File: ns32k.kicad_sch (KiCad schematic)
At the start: 52 parts, among them SW2 SW_DIP_x04, U1 NS32201, U10 74AHC373, U11 74AHC373, U12 74AHC138, U13 AS6C6416-55, U15 MX29LV040C, U16 MX29LV040C, U19 74AHC138, U20 74AHC1G08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

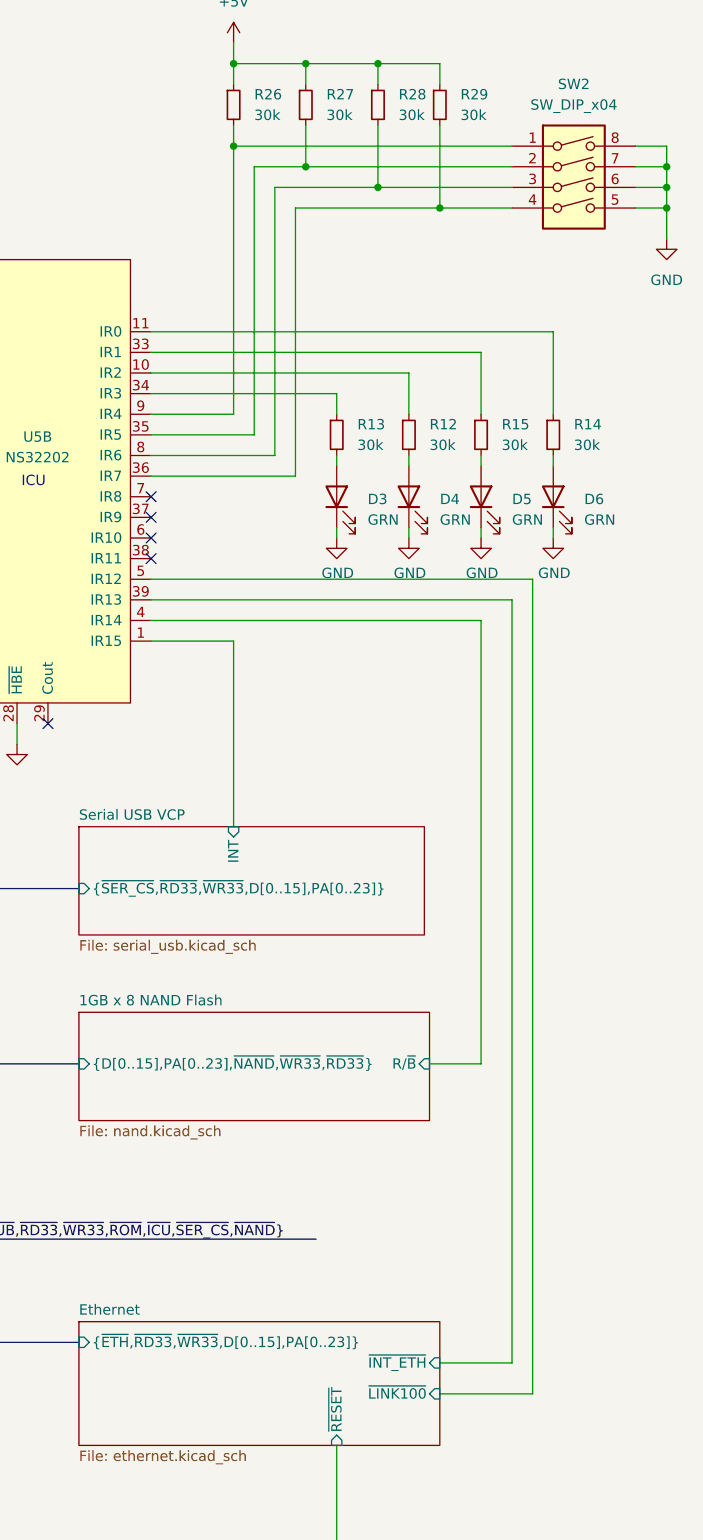
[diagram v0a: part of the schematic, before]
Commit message: use ICU even pins for GPIO
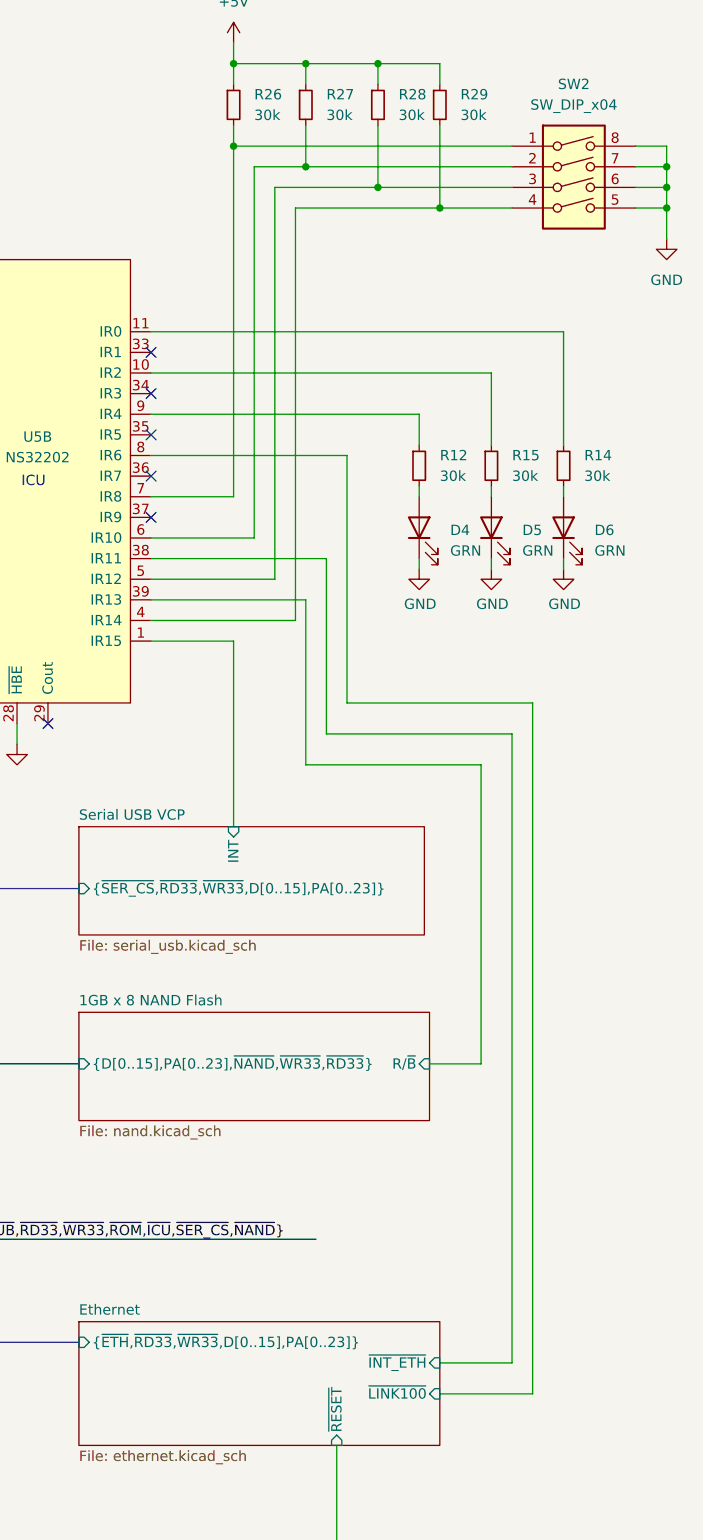
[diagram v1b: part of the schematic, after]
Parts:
- removed D3: GRN, Diode_SMD:D_0603_1608Metric, symbol Device:LED
- removed R13: 30k, Resistor_SMD:R_0402_1005Metric, symbol Device:R_Small
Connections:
- net 1GB x 8 NAND Flash/R/~{B}: now also U5.39 (IR13); no longer U5.4 (IR14)
- net Ethernet/~{INT_ETH}: now also U5.38 (IR11); no longer U5.39 (IR13)
- net Ethernet/~{LINK100}: now also U5.8 (IR6); no longer U5.5 (IR12)
- net at R26.2, SW2.1: now also U5.7 (IR8); no longer U5.9 (IR4)
- net at R27.2, SW2.2: now also U5.6 (IR10); no longer U5.35 (IR5)
- net at R28.2, SW2.3: now also U5.5 (IR12); no longer U5.8 (IR6)
- net at R29.2, SW2.4: now also U5.4 (IR14); no longer U5.36 (IR7)
- net at R15.1: now also U5.10 (IR2); no longer U5.33 (IR1)
- net at R12.1: now also U5.9 (IR4); no longer U5.10 (IR2)
- no-connect marks 18 -> 19
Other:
- moved on the sheet: D4, D5, D6, R12, R14, R15

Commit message: add jumpers, much cleanup
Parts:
- added R13, R41: 0R, Resistor_SMD:R_0402_1005Metric, symbol Device:R_Small
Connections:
- net PA5: now also R41.1
- net ST1: now also R13.1; no longer U5.3 (ST1)
- new net: R13.2, R41.2, U5.3 (ST1)
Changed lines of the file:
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@@
 	)
 	(junction
+		(at 290.83 52.07)
+		(diameter 0)
+		(color 0 0 0 0)
+	)
+	(junction
 		(at 219.71 151.13)
 		(diameter 0)
@@
 	)
 	(bus_entry
+		(at 293.37 73.66)
+		(size -2.54 -2.54)
+		(stroke
+			(width 0)
+			(type default)
+		)
+	)
+	(bus_entry
 		(at 205.74 114.3)
 		(size 2.54 2.54)
@@
 	)
 	(bus_entry
-		(at 270.51 76.2)
+		(at 245.11 76.2)
 		(size 2.54 -2.54)
 		(stroke
@@
 	(bus
 		(pts
-			(xy 262.89 76.2) (xy 265.43 76.2)
-		)
-		(stroke
-			(width 0)
-			(type default)
-		)
-	)
-	(bus
-		(pts
 			(xy 293.37 125.73) (xy 293.37 114.3)
 		)
@@
 	(bus
 		(pts
+			(xy 267.97 76.2) (xy 271.78 76.2)
+		)
+		(stroke
+			(width 0)
+			(type default)
+		)
+	)
+	(bus
+		(pts
 			(xy 106.68 76.2) (xy 109.22 76.2)
 		)
@@
 		)
 	)
+	(bus
+		(pts
+			(xy 266.7 76.2) (xy 267.97 76.2)
+		)
+		(stroke
+			(width 0)
+			(type default)
+		)
+	)
 	(wire
 		(pts
@@
 	(bus
 		(pts
-			(xy 293.37 72.39) (xy 293.37 74.93)
+			(xy 293.37 72.39) (xy 293.37 73.66)
 		)
 		(stroke
@@
 	(bus
 		(pts
-			(xy 220.98 76.2) (xy 250.19 76.2)
+			(xy 220.98 76.2) (xy 245.11 76.2)
 		)
 		(stroke
@@
 		)
 	)
+	(wire
+		(pts
+			(xy 290.83 52.07) (xy 303.53 52.07)
+		)
+		(stroke
+			(width 0)
+			(type default)
+		)
+	)
 	(bus
 		(pts
@@
 		)
 	)
+	(bus
+		(pts
+			(xy 250.19 76.2) (xy 245.11 76.2)
+		)
+		(stroke
+			(width 0)
+			(type default)
+		)
+	)
 	(wire
 		(pts
@@
 		)
 	)
-	(bus
-		(pts
-			(xy 266.7 76.2) (xy 267.97 76.2)
-		)
-		(stroke
-			(width 0)
-			(type default)
-		)
-	)
 	(wire
 		(pts
@@
 		)
 	)
-	(bus
-		(pts
-			(xy 250.19 76.2) (xy 252.73 76.2)
-		)
-		(stroke
-			(width 0)
-			(type default)
-		)
-	)
 	(wire
 		(pts
@@
 	(bus
 		(pts
+			(xy 252.73 76.2) (xy 250.19 76.2)
+		)
+		(stroke
+			(width 0)
+			(type default)
+		)
+	)
+	(bus
+		(pts
 			(xy 190.5 246.38) (xy 193.04 246.38)
 		)
@@
 		)
 	)
-	(bus
-		(pts
-			(xy 252.73 76.2) (xy 255.27 76.2)
-		)
-		(stroke
-			(width 0)
-			(type default)
-		)
-	)
 	(wire
 		(pts
@@
 	(bus
 		(pts
-			(xy 267.97 76.2) (xy 270.51 76.2)
-		)
-		(stroke
-			(width 0)
-			(type default)
-		)
-	)
-	(bus
-		(pts
 			(xy 139.7 114.3) (xy 142.24 114.3)
 		)
@@
 		)
 	)
+	(wire
+		(pts
+			(xy 290.83 52.07) (xy 290.83 58.42)
+		)
+		(stroke
+			(width 0)
+			(type default)
+		)
+	)
 	(bus
 		(pts
@@
 		)
 	)
+	(wire
+		(pts
+			(xy 255.27 52.07) (xy 290.83 52.07)
+		)
+		(stroke
+			(width 0)
+			(type default)
+		)
+	)
 	(bus
 		(pts
@@
 	(bus
 		(pts
-			(xy 270.51 76.2) (xy 271.78 76.2)
-		)
-		(stroke
-			(width 0)
-			(type default)
-		)
-	)
-	(bus
-		(pts
 			(xy 162.56 76.2) (xy 163.83 76.2)
 		)
@@
 		)
 	)
+	(bus
+		(pts
+			(xy 255.27 76.2) (xy 252.73 76.2)
+		)
+		(stroke
+			(width 0)
+			(type default)
+		)
+	)
 	(wire
 		(pts
@@
 	(bus
 		(pts
+			(xy 265.43 76.2) (xy 262.89 76.2)
+		)
+		(stroke
+			(width 0)
+			(type default)
+		)
+	)
+	(bus
+		(pts
 			(xy 157.48 76.2) (xy 158.75 76.2)
 		)
@@
 	(wire
 		(pts
-			(xy 273.05 52.07) (xy 303.53 52.07)
+			(xy 247.65 52.07) (xy 250.19 52.07)
 		)
 		(stroke
@@
 		)
 	)
+	(bus
+		(pts
+			(xy 257.81 76.2) (xy 255.27 76.2)
+		)
+		(stroke
+			(width 0)
+			(type default)
+		)
+	)
 	(wire
 		(pts
@@
 	(wire
 		(pts
+			(xy 290.83 63.5) (xy 290.83 71.12)
+		)
+		(stroke
+			(width 0)
+			(type default)
+		)
+	)
+	(bus
+		(pts
+			(xy 293.37 73.66) (xy 293.37 74.93)
+		)
+		(stroke
+			(width 0)
+			(type default)
+		)
+	)
+	(wire
+		(pts
 			(xy 355.6 24.13) (xy 355.6 26.67)
 		)
@@
 	(wire
 		(pts
-			(xy 273.05 73.66) (xy 273.05 52.07)
+			(xy 247.65 73.66) (xy 247.65 52.07)
 		)
 		(stroke
@@
 		)
 	)
-	(bus
-		(pts
-			(xy 255.27 76.2) (xy 257.81 76.2)
-		)
-		(stroke
-			(width 0)
-			(type default)
-		)
-	)
 	(wire
 		(pts
@@
 		)
 	)
+	(label "PA5"
+		(at 290.83 71.12 90)
+		(effects
+			(font
+				(size 1.27 1.27)
+			)
+			(justify left bottom)
+		)
+	)
 	(label "D6"
 		(at 118.11 123.19 0)
@@
 	)
 	(label "ST1"
-		(at 273.05 72.39 90)
+		(at 247.65 72.39 90)
 		(fields_autoplaced yes)
 		(effects
@@
 	)
 	(symbol
+		(lib_id "Device:R_Small")
+		(at 252.73 52.07 90)
+		(unit 1)
+		(exclude_from_sim no)
+		(in_bom yes)
+		(on_board yes)
+		(dnp no)
+		(fields_autoplaced yes)
+		(property "Reference" "R13"
+			(at 252.73 46.99 90)
+			(effects
+				(font
+					(size 1.27 1.27)
+				)
+			)
+		)
+		(property "Value" "0R"
+			(at 252.73 49.53 90)
+			(effects
+				(font
+					(size 1.27 1.27)
+				)
+			)
+		)
+		(property "Footprint" "Resistor_SMD:R_0402_1005Metric"
+			(at 252.73 52.07 0)
+			(effects
+				(font
+					(size 1.27 1.27)
+				)
+				(hide yes)
+			)
+		)
+		(property "Datasheet" "~"
+			(at 252.73 52.07 0)
+			(effects
+				(font
+					(size 1.27 1.27)
+				)
+				(hide yes)
+			)
+		)
+		(property "Description" "Resistor, small symbol"
+			(at 252.73 52.07 0)
+			(effects
+				(font
+					(size 1.27 1.27)
+				)
+				(hide yes)
+			)
+		)
+		(pin "1"
+		)
+		(pin "2"
+		)
+		(instances
+			(project "ns32k"
+				(path "/54787df0-1b8c-465f-acae-f55ec7f02da3"
+					(reference "R13")
+					(unit 1)
+				)
+			)
+		)
+	)
+	(symbol
 		(lib_id "NS32K_chipset:NS32202")
 		(at 322.58 67.31 0)
@@
 					(unit 1)
 				)
+			)
+		)
+	)
+	(symbol
+		(lib_id "Device:R_Small")
+		(at 290.83 60.96 0)
+		(mirror x)
+		(unit 1)
+		(exclude_from_sim no)
+		(in_bom yes)
+		(on_board yes)
+		(dnp yes)
+		(property "Reference" "R41"
+			(at 288.29 59.6899 0)
+			(effects
+				(font
+					(size 1.27 1.27)
+				)
+				(justify right)
+			)
+		)
+		(property "Value" "0R"
+			(at 288.29 62.2299 0)
+			(effects
+				(font
+					(size 1.27 1.27)
+				)
+				(justify right)
+			)
+		)
+		(property "Footprint" "Resistor_SMD:R_0402_1005Metric"
+			(at 290.83 60.96 0)
+			(effects
+				(font
+					(size 1.27 1.27)
+				)
+				(hide yes)
+			)
+		)
+		(property "Datasheet" "~"
+			(at 290.83 60.96 0)
+			(effects
+				(font
+					(size 1.27 1.27)
+				)
+				(hide yes)
+			)
+		)
+		(property "Description" "Resistor, small symbol"
+			(at 290.83 60.96 0)
+			(effects
+				(font
+					(size 1.27 1.27)
+				)
+				(hide yes)
+			)
+		)
+		(pin "1"
+		)
+		(pin "2"
+		)
+		(instances
+			(project "ns32k"
+				(path "/54787df0-1b8c-465f-acae-f55ec7f02da3"
+					(reference "R41")
+					(unit 1)
+				)

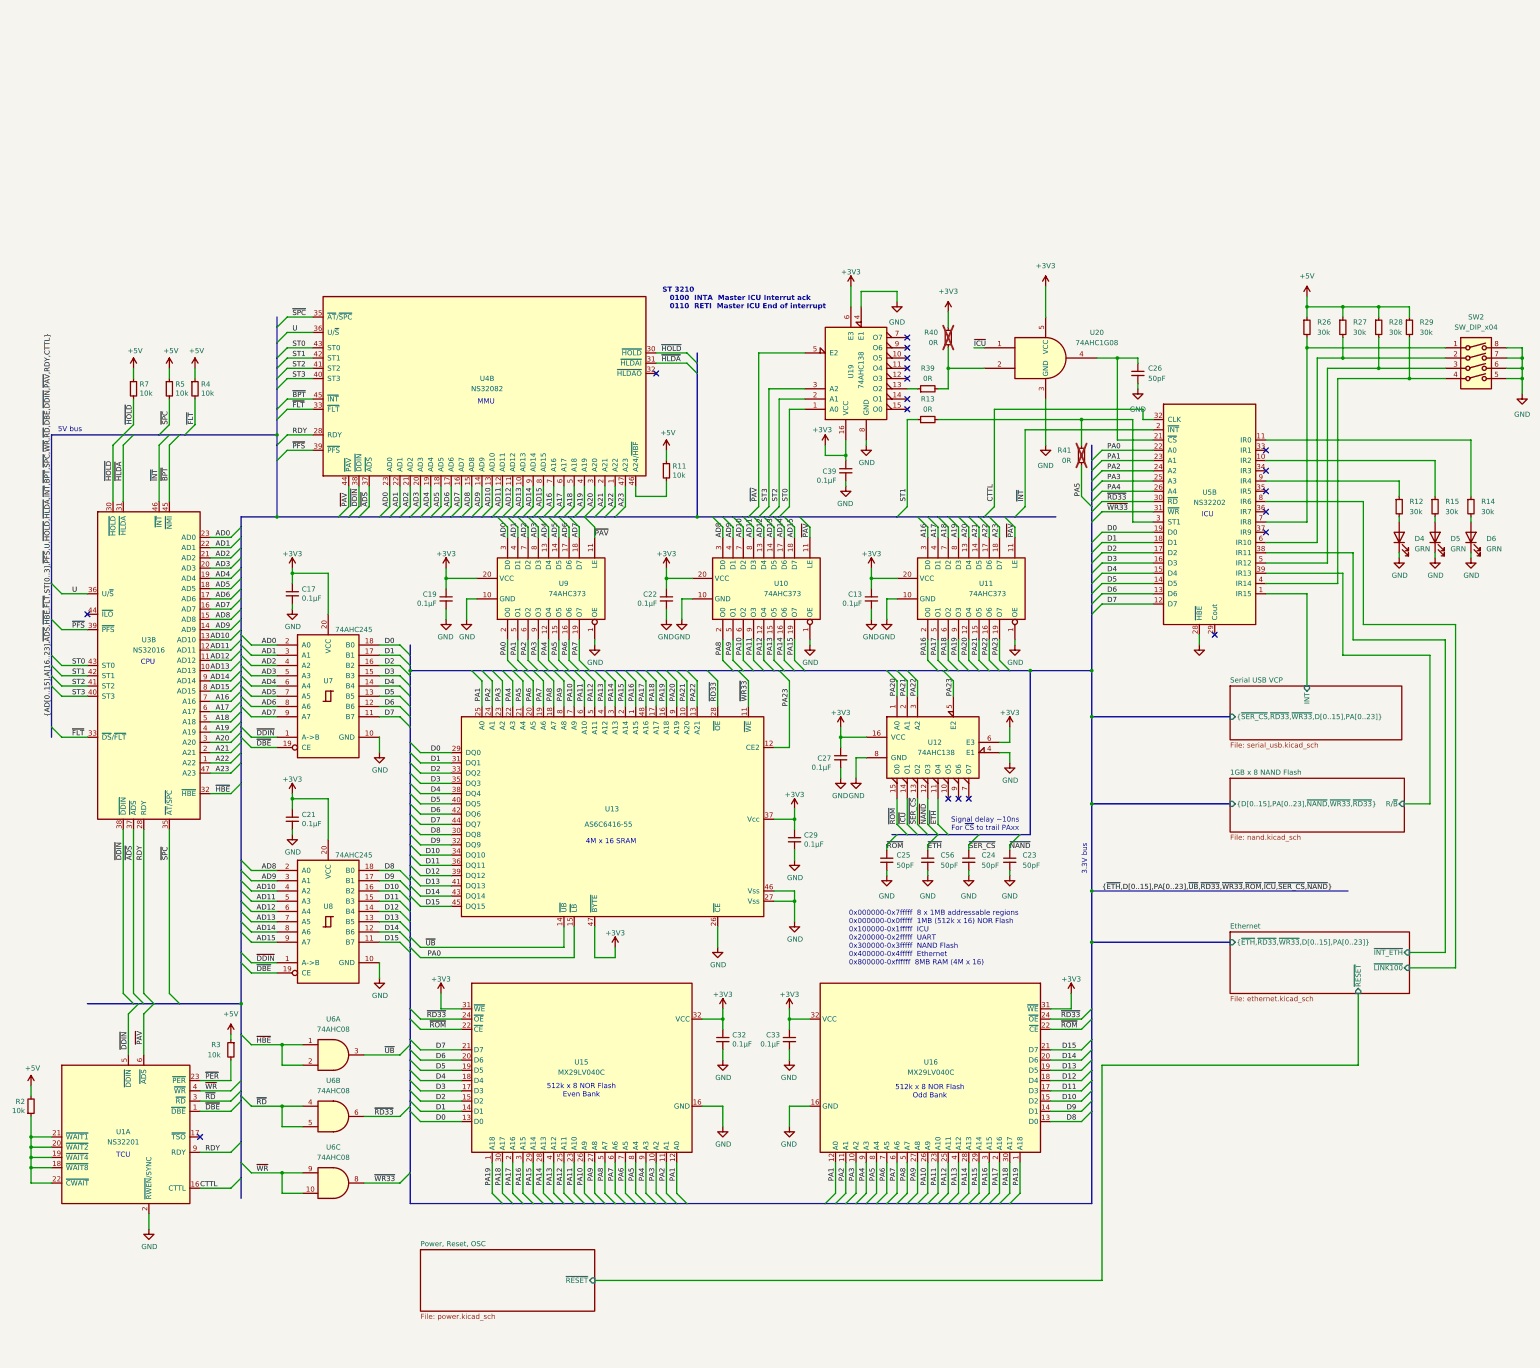
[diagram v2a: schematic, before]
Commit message: add buffer to ICU
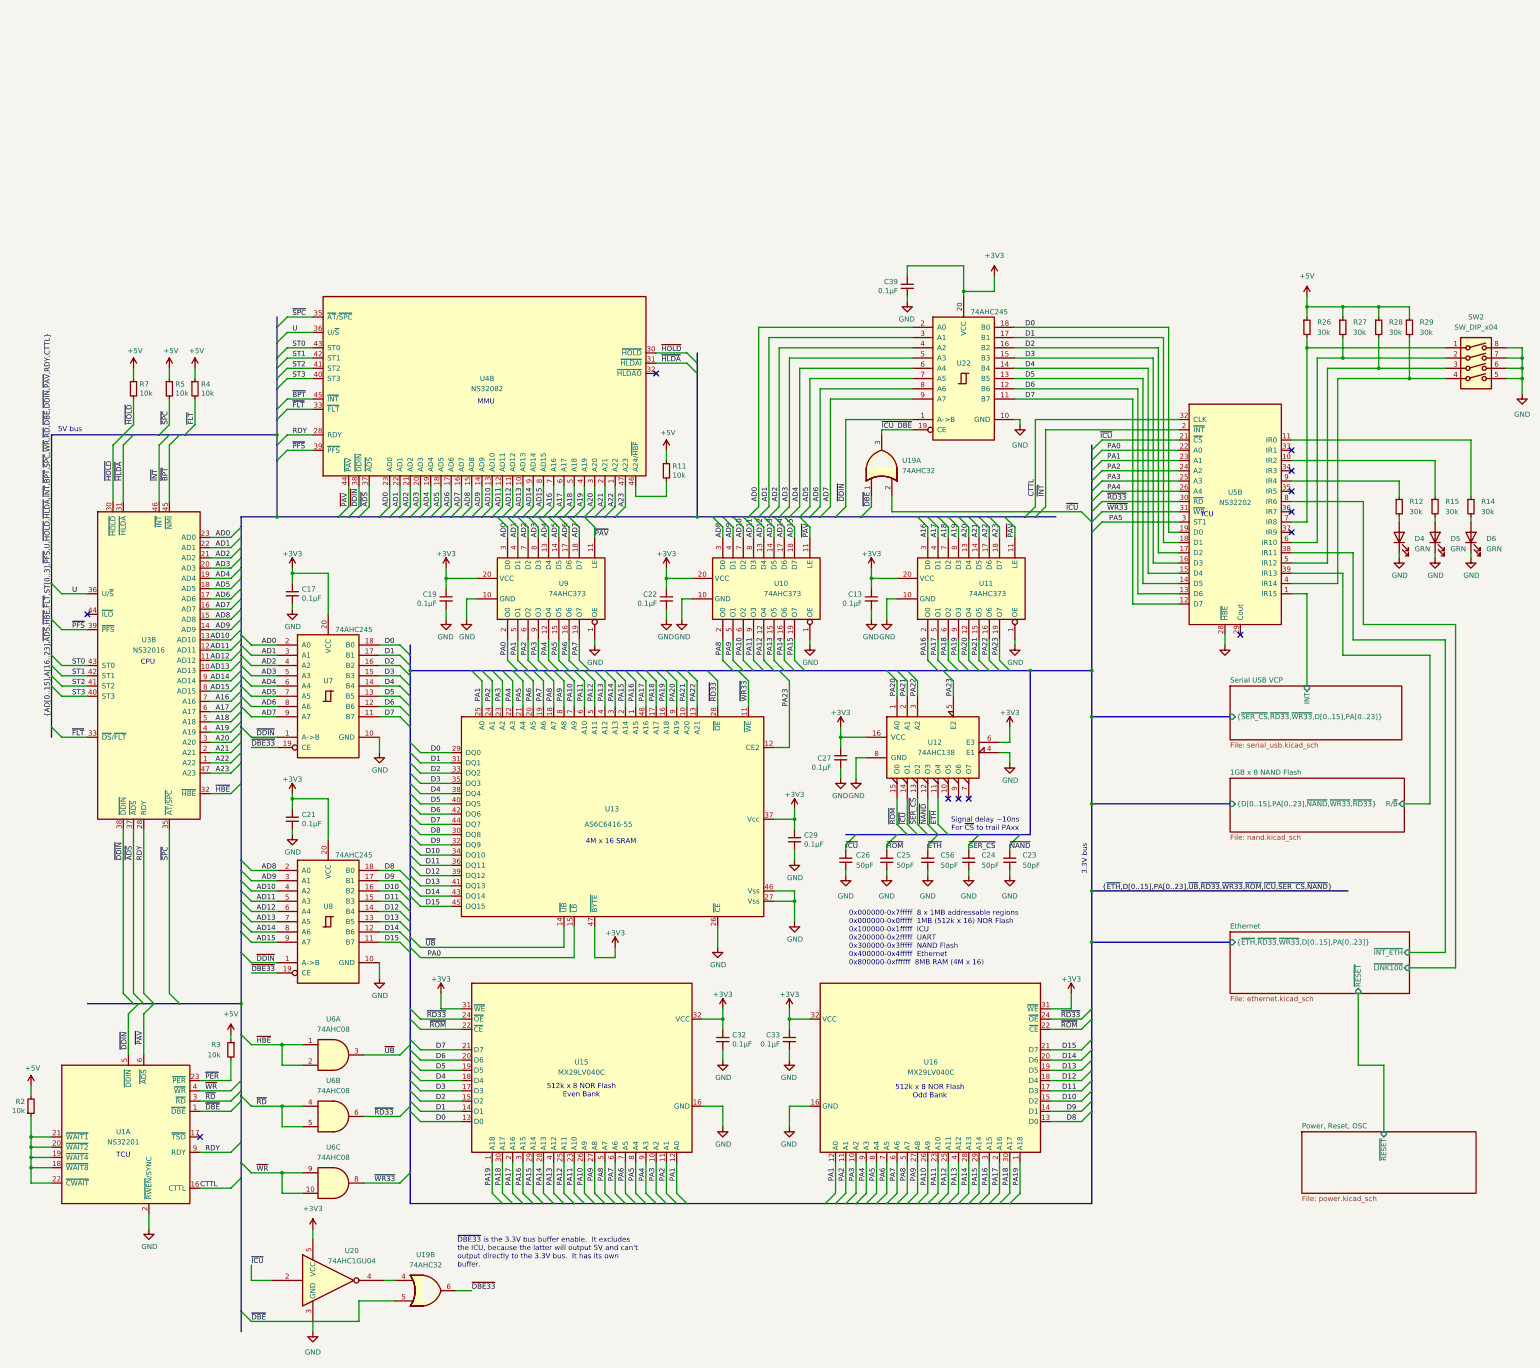
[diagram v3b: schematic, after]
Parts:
- removed R13, R39, R40, R41: 0R, Resistor_SMD:R_0402_1005Metric, symbol Device:R_Small
- removed U19: 74AHC138, Package_SO:TSSOP-16_4.4x5mm_P0.65mm, symbol 74AHC138:74AHC138
- removed U20: 74AHC1G08, Package_TO_SOT_SMD:SOT-23-5, symbol 74xGxx:74AHC1G08
- added U19: 74AHC32, Package_SO:TSSOP-14_4.4x5mm_P0.65mm, symbol 74xx:74LS32
- added U20: 74AHC1GU04, Package_TO_SOT_SMD:SOT-23-5, symbol 74xGxx:74AHC1GU04
- added U22: 74AHC245, Package_SO:TSSOP-20_4.4x6.5mm_P0.65mm, symbol 74AHC245:74HC245
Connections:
- net +3V3: now also U20.5 (VCC), U22.20 (VCC)
- net AD0: now also U22.2 (A0)
- net AD1: now also U22.3 (A1)
- net AD2: now also U22.4 (A2)
- net AD3: now also U22.5 (A3)
- net AD4: now also U22.6 (A4)
- net AD5: now also U22.7 (A5)
- net AD6: now also U22.8 (A6)
- net AD7: now also U22.9 (A7)
- net D0: now also U22.18 (B0)
- net D1: now also U22.17 (B1)
- net D2: now also U22.16 (B2)
- net D3: now also U22.15 (B3)
- net D4: now also U22.14 (B4)
- net D5: now also U22.13 (B5)
- net D6: now also U22.12 (B6)
- net D7: now also U22.11 (B7)
- net GND: now also U20.3 (GND), U22.10 (GND)
- net PA5: now also U5.3 (ST1)
- net ~{DBE}: now also U19.1, U19.5; no longer U7.19 (CE), U8.19 (CE)
- net ~{DDIN}: now also U22.1 (A->B)
- net ~{ICU}: now also C26.1, U5.21 (~{CS}), U19.2, U20.2
- new net: U19.4, U20.4
- new net ~{DBE33}: U19.6, U7.19 (CE), U8.19 (CE)
- new net ~{ICU_DBE}: U19.3, U22.19 (CE)
- no-connect marks 19 -> 12
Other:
- note added: "~{DBE33} is the 3.3V bus buffer enable. It excludes the ICU, because the latter will output 5V and can't output directly to the 3.3V bus. It has its own buffer."
- note removed: "ST 3210 0100 INTA Master ICU Interrut ack 0110 RETI Master ICU End of interrupt"
- moved on the sheet: U5B
